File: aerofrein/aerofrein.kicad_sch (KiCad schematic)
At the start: 13 parts, among them J1 MS1, J2 MS2, J3 endstop, J4 comm, J5 motor, J6 power, J7 HMI, U1 RP2040, U3 TMC2209

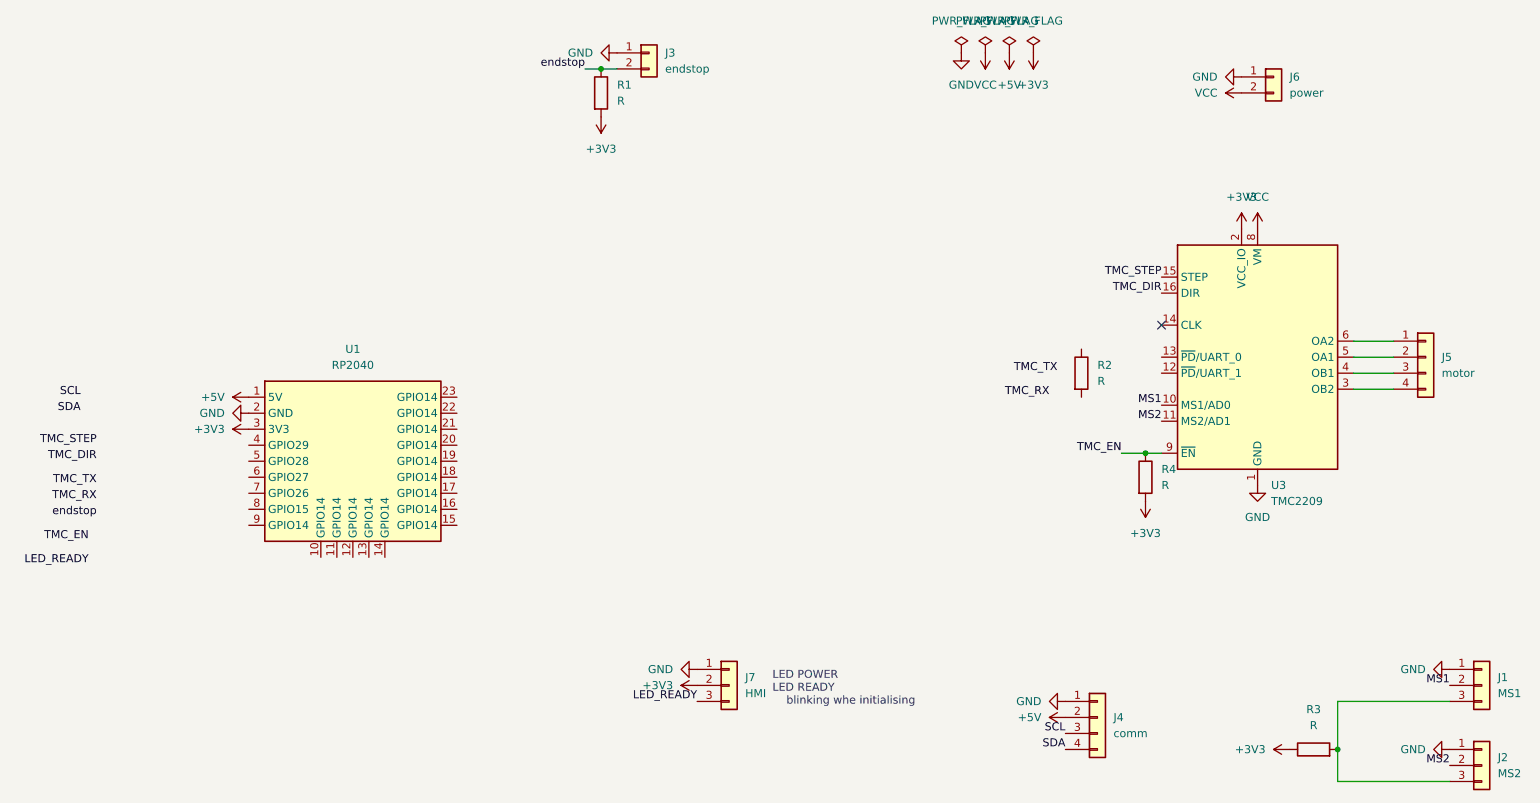
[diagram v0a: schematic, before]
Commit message: finition des aérofreins
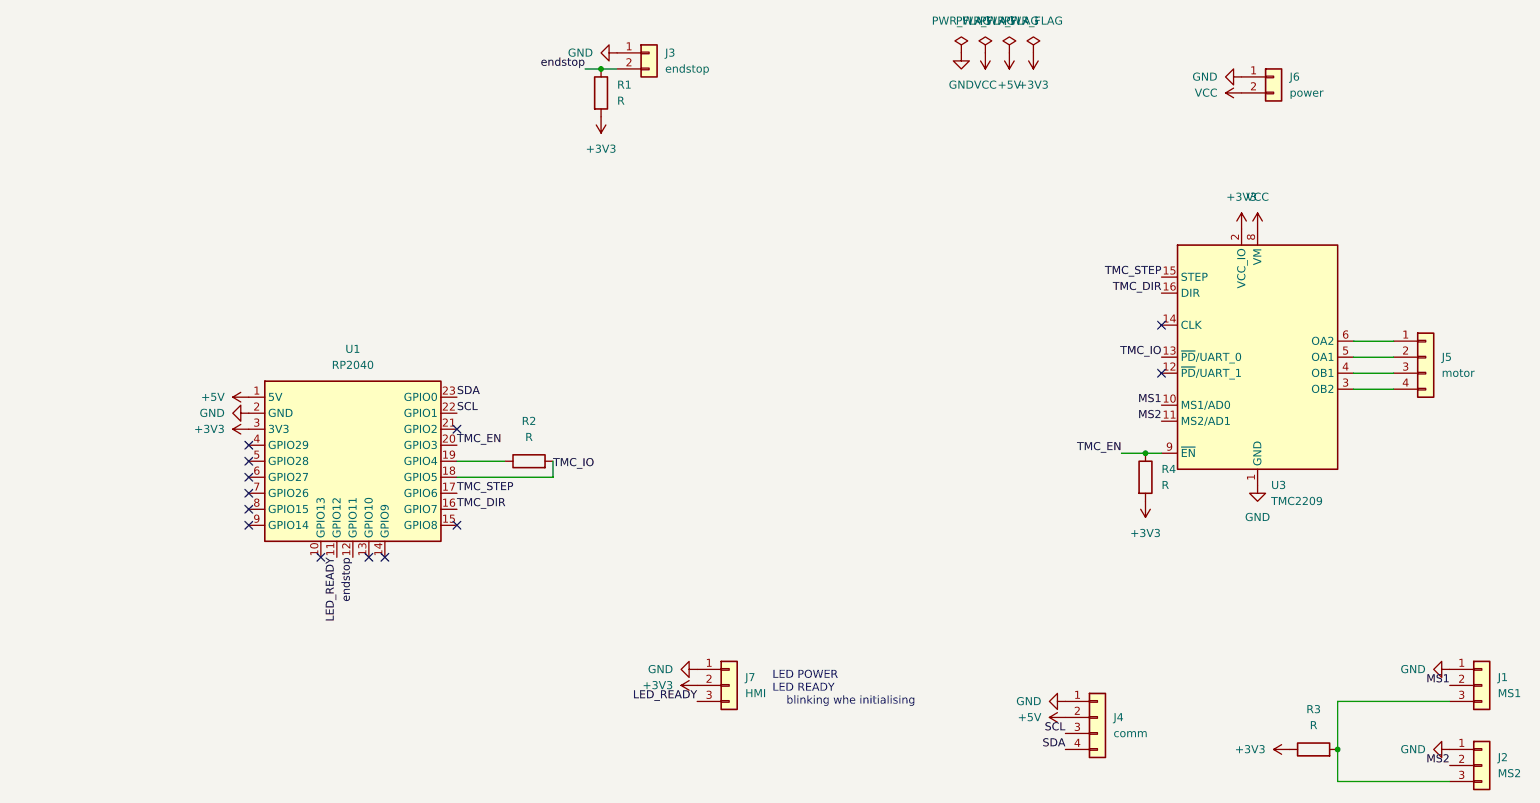
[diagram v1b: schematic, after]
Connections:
- net LED_READY: now also U1.11 (GPIO12)
- net SCL: now also U1.22 (GPIO1)
- net SDA: now also U1.23 (GPIO0)
- net TMC_DIR: now also U1.16 (GPIO7)
- net TMC_EN: now also U1.20 (GPIO3)
- net TMC_STEP: now also U1.17 (GPIO6)
- net endstop: now also U1.12 (GPIO11)
- net TMC_IO: now reaches U1.18 (GPIO5)
- net TMC_IO: now also R2.2, U3.13 (~{PD}/UART_0)
- net at U1.19 (GPIO4): now also R2.1
- no-connect marks 1 -> 13
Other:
- moved on the sheet: R2
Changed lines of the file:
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@@
+	)
+	(no_connect
+		(at 58.42 106.68)
+	)
+	(no_connect
+		(at 58.42 111.76)
+	)
+	(no_connect
+		(at 58.42 101.6)
+	)
+	(no_connect
+		(at 58.42 109.22)
+	)
+	(no_connect
+		(at 58.42 104.14)
+	)
+	(no_connect
+		(at 80.01 119.38)
+	)
+	(no_connect
+		(at 91.44 114.3)
+	)
+	(no_connect
+		(at 77.47 119.38)
+	)
+	(no_connect
+		(at 91.44 99.06)
+	)
+	(no_connect
+		(at 58.42 114.3)
+	)
+	(no_connect
+		(at 203.2 90.17)
 	)
 	(no_connect
 		(at 203.2 82.55)
+	)
+	(no_connect
+		(at 69.85 119.38)
 	)
 	(wire
@@
 	(wire
 		(pts
-			(xy 111.76 41.91) (xy 114.3 41.91)
+			(xy 106.68 106.68) (xy 106.68 104.14)
 		)
 		(stroke
@@
 	(wire
 		(pts
-			(xy 233.68 87.63) (xy 240.03 87.63)
+			(xy 91.44 104.14) (xy 99.06 104.14)
 		)
 		(stroke
@@
 	(wire
 		(pts
-			(xy 231.14 142.24) (xy 231.14 149.86)
+			(xy 111.76 41.91) (xy 114.3 41.91)
 		)
 		(stroke
@@
 		)
 	)
+	(wire
+		(pts
+			(xy 233.68 87.63) (xy 240.03 87.63)
+		)
+		(stroke
+			(width 0)
+			(type default)
+		)
+	)
+	(wire
+		(pts
+			(xy 91.44 106.68) (xy 106.68 106.68)
+		)
+		(stroke
+			(width 0)
+			(type default)
+		)
+	)
+	(wire
+		(pts
+			(xy 231.14 142.24) (xy 231.14 149.86)
+		)
+		(stroke
+			(width 0)
+			(type default)
+		)
+	)
 	(label "MS1"
 		(at 248.92 139.7 180)
@@
 		)
 	)
-	(label "TMC_TX"
-		(at 186.69 90.17 180)
+	(label "TMC_IO"
+		(at 203.2 87.63 180)
 		(effects
 			(font
@@
 	)
 	(label "LED_READY"
-		(at 33.02 120.65 180)
+		(at 72.39 119.38 270)
 		(effects
 			(font
@@
 	)
 	(label "TMC_EN"
-		(at 33.02 116.84 180)
-		(effects
-			(font
-				(size 1.27 1.27)
-			)
-			(justify right bottom)
+		(at 91.44 101.6 0)
+		(effects
+			(font
+				(size 1.27 1.27)
+			)
+			(justify left bottom)
+		)
+	)
+	(label "TMC_IO"
+		(at 106.68 105.41 0)
+		(effects
+			(font
+				(size 1.27 1.27)
+			)
+			(justify left bottom)
 		)
 	)
@@
 	)
 	(label "TMC_STEP"
-		(at 34.29 101.6 180)
-		(effects
-			(font
-				(size 1.27 1.27)
-			)
-			(justify right bottom)
+		(at 91.44 109.22 0)
+		(effects
+			(font
+				(size 1.27 1.27)
+			)
+			(justify left bottom)
 		)
 	)
@@
 	)
 	(label "endstop"
-		(at 34.29 113.03 180)
+		(at 74.93 119.38 270)
 		(effects
 			(font
@@
 		)
 	)
-	(label "TMC_TX"
-		(at 34.29 107.95 180)
-		(effects
-			(font
-				(size 1.27 1.27)
-			)
-			(justify right bottom)
-		)
-	)
-	(label "TMC_RX"
-		(at 34.29 110.49 180)
-		(effects
-			(font
-				(size 1.27 1.27)
-			)
-			(justify right bottom)
-		)
-	)
 	(label "TMC_STEP"
 		(at 203.2 74.93 180)
@@
 		)
 	)
-	(label "TMC_RX"
-		(at 185.42 93.98 180)
-		(effects
-			(font
-				(size 1.27 1.27)
-			)
-			(justify right bottom)
-		)
-	)
 	(label "TMC_DIR"
-		(at 34.29 104.14 180)
-		(effects
-			(font
-				(size 1.27 1.27)
-			)
-			(justify right bottom)
+		(at 91.44 111.76 0)
+		(effects
+			(font
+				(size 1.27 1.27)
+			)
+			(justify left bottom)
 		)
 	)
 	(label "SCL"
-		(at 31.75 93.98 180)
-		(effects
-			(font
-				(size 1.27 1.27)
-			)
-			(justify right bottom)
+		(at 91.44 96.52 0)
+		(effects
+			(font
+				(size 1.27 1.27)
+			)
+			(justify left bottom)
 		)
 	)
@@
 	)
 	(label "SDA"
-		(at 31.75 96.52 180)
-		(effects
-			(font
-				(size 1.27 1.27)
-			)
-			(justify right bottom)
+		(at 91.44 93.98 0)
+		(effects
+			(font
+				(size 1.27 1.27)
+			)
+			(justify left bottom)
 		)
 	)
@@
 	(symbol
 		(lib_id "Device:R")
-		(at 190.5 90.17 0)
+		(at 102.87 104.14 90)
 		(unit 1)
 		(exclude_from_sim no)
@@
 		(fields_autoplaced yes)
 		(property "Reference" "R2"
-			(at 193.04 88.8999 0)
-			(effects
-				(font
-					(size 1.27 1.27)
-				)
-				(justify left)
+			(at 102.87 97.79 90)
+			(effects
+				(font
+					(size 1.27 1.27)
+				)
 			)
 		)
 		(property "Value" "R"
-			(at 193.04 91.4399 0)
-			(effects
-				(font
-					(size 1.27 1.27)
-				)
-				(justify left)
-			)
-		)
-		(property "Footprint" ""
-			(at 188.722 90.17 90)
+			(at 102.87 100.33 90)
+			(effects
+				(font
+					(size 1.27 1.27)
+				)
+			)
+		)
+		(property "Footprint" ""
+			(at 102.87 105.918 90)
 			(effects
 				(font
@@
 		)
 		(property "Datasheet" "~"
-			(at 190.5 90.17 0)
+			(at 102.87 104.14 0)
 			(effects
 				(font
@@
 		)
 		(property "Description" "Resistor"
-			(at 190.5 90.17 0)
-			(effects
-				(font
+			(at 102.87 104.14 0)
+			(effects
+				(font

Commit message: Update airbrakes PCB
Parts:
- J1: renamed from J3; footprint (none) -> Connector_JST:JST_XH_B2B-XH-A_1x02_P2.50mm_Vertical
- J2: renamed from J7; footprint (none) -> Connector_JST:JST_XH_B3B-XH-A_1x03_P2.50mm_Vertical
- J3: renamed from J4; footprint (none) -> Connector_JST:JST_XH_B4B-XH-A_1x04_P2.50mm_Vertical
- J4: renamed from J6; footprint (none) -> Connector_JST:JST_XH_B2B-XH-A_1x02_P2.50mm_Vertical
- J5: footprint (none) -> Connector_JST:JST_XH_B4B-XH-A_1x04_P2.50mm_Vertical
- J6: renamed from J1; footprint (none) -> Connector_PinHeader_2.54mm:PinHeader_1x03_P2.54mm_Vertical
- J7: renamed from J2; footprint (none) -> Connector_PinHeader_2.54mm:PinHeader_1x03_P2.54mm_Vertical
- R1: renamed from R2; footprint (none) -> Resistor_THT:R_Axial_DIN0204_L3.6mm_D1.6mm_P7.62mm_Horizontal
- R2: renamed from R1; footprint (none) -> Resistor_THT:R_Axial_DIN0204_L3.6mm_D1.6mm_P7.62mm_Horizontal
- R3: renamed from R4; footprint (none) -> Resistor_THT:R_Axial_DIN0204_L3.6mm_D1.6mm_P7.62mm_Horizontal
- R4: renamed from R3; footprint (none) -> Resistor_THT:R_Axial_DIN0204_L3.6mm_D1.6mm_P7.62mm_Horizontal
- renumbered U3 to U2

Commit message: création de la carte PCB aérofrein
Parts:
- removed J6: MS1, Connector_PinHeader_2.54mm:PinHeader_1x03_P2.54mm_Vertical, symbol Connector_Generic:Conn_01x03
- removed J7: MS2, Connector_PinHeader_2.54mm:PinHeader_1x03_P2.54mm_Vertical, symbol Connector_Generic:Conn_01x03
- added J4: MSX, Connector_PinHeader_2.54mm:PinHeader_2x03_P2.54mm_Vertical, symbol Connector_Generic:Conn_02x03_Odd_Even
- R1, R4: value R -> 1k
- R2, R3: value R -> 10k
- renumbered J4 to J5, J5 to J6
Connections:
- net GND: now also J4.1 (Pin_1), J4.2 (Pin_2)
- net LED_READY: now also U1.10 (GPIO13); no longer U1.11 (GPIO12)
- net MS1: now also J4.3 (Pin_3)
- net MS2: now also J4.4 (Pin_4)
- net SCL: now also U1.11 (GPIO12); no longer U1.22 (GPIO1)
- net SDA: now also U1.12 (GPIO11); no longer U1.23 (GPIO0)
- net TMC_DIR: now also U1.15 (GPIO8); no longer U1.16 (GPIO7)
- net TMC_STEP: now also U1.16 (GPIO7); no longer U1.17 (GPIO6)
- net ENDSTOP: now reaches U1.14 (GPIO9)
- net ENDSTOP: now also J1.2 (Pin_2), R2.1
- net at R4.2: now also J4.5 (Pin_5), J4.6 (Pin_6)
- removed net endstop: J1.2 (Pin_2), R2.1, U1.12 (GPIO11)
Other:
- moved on the sheet: R4
